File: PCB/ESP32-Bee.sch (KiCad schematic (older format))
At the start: 33 parts, among them J1 M22-2511005, J2 M22-2511005, SW1 B3U-1000P, T1 1909763-1, U1 ESP32, U2 W25Q64FWSSIG, X1 FA-128_26.0000MF10Z-AC3

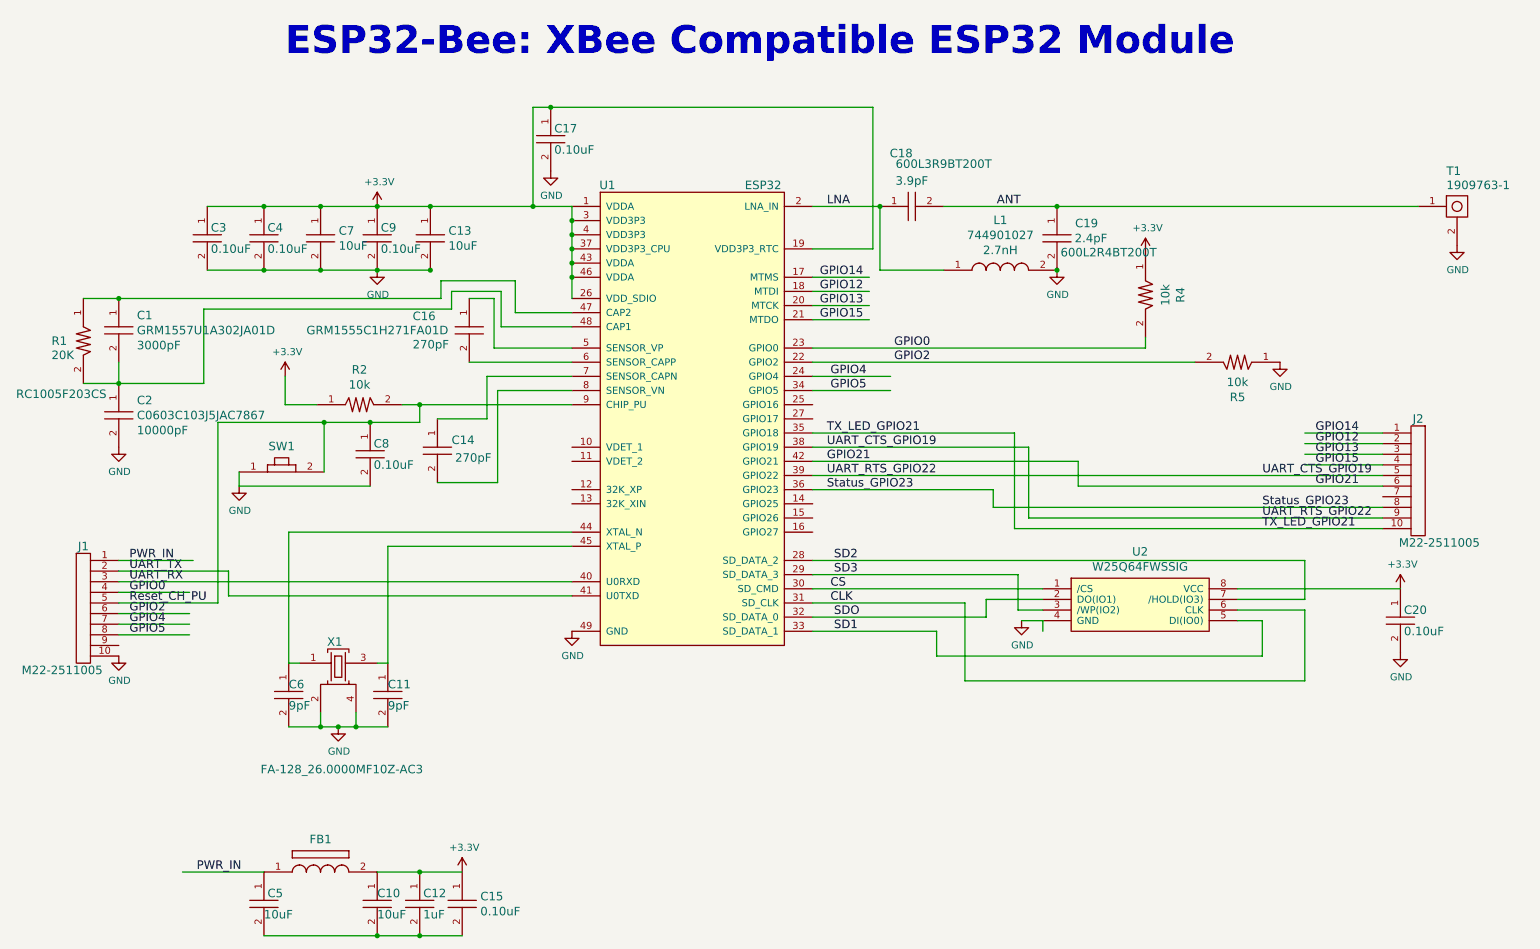
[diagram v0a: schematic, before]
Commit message: More Progress
More progress with the PCB, having a hard time finding a RF shielf that
is XBee pro sized.
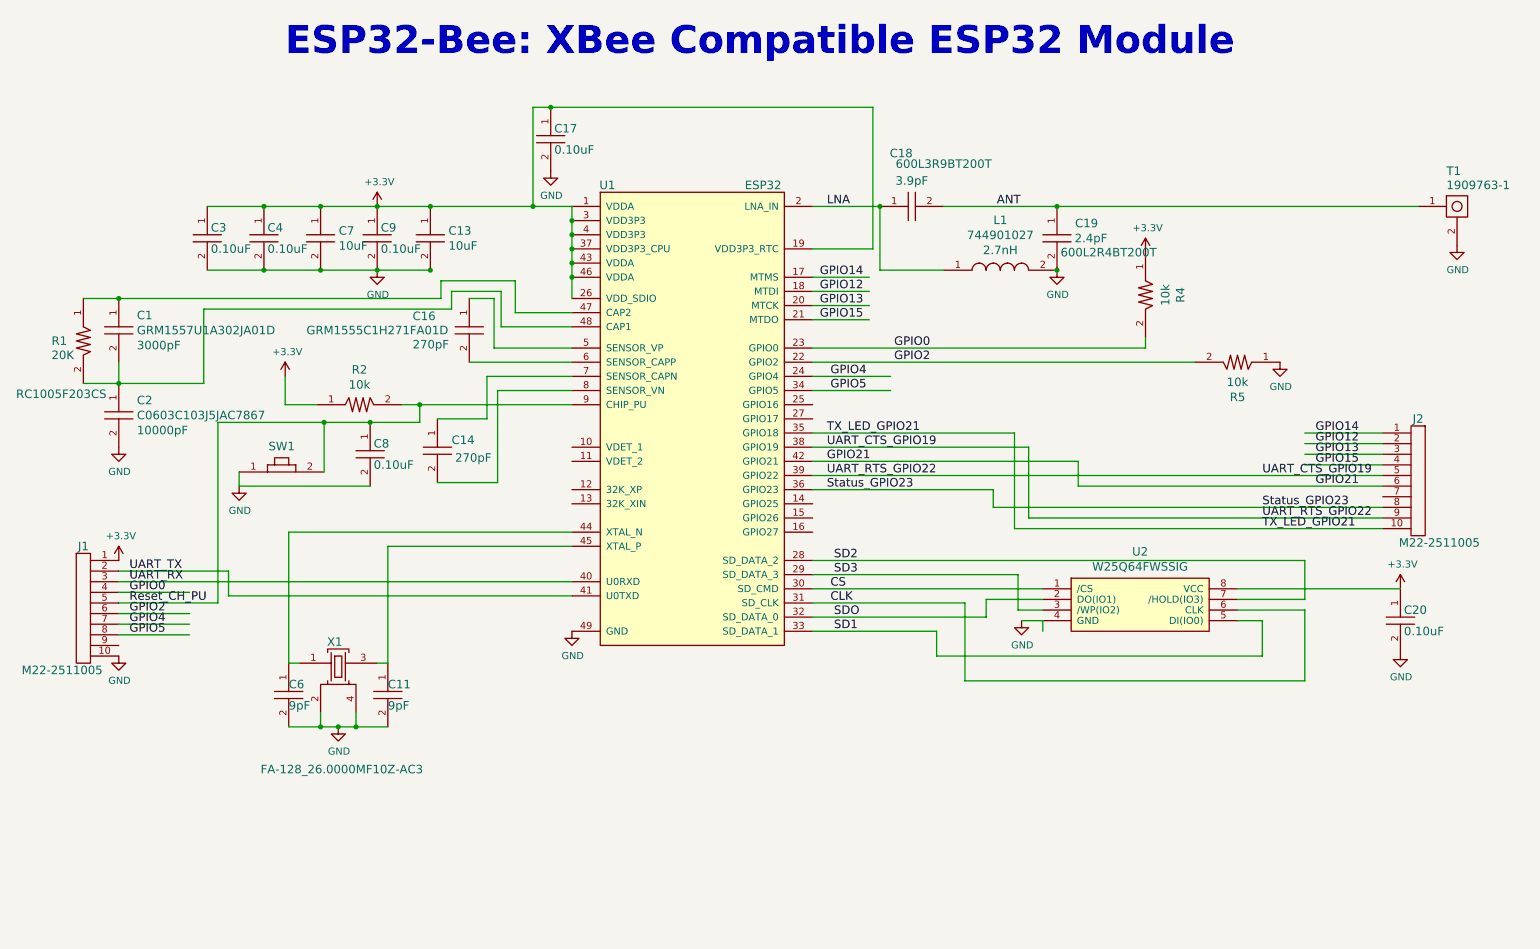
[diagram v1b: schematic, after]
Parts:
- removed C10, C5: CL10A106KQ8NNNC, PCB_Footprints:C0603, symbol CL10A106KQ8NNNC
- removed C12: CL05A105KA5NQNC, PCB_Footprints:C0402, symbol CL05A105KA5NQNC
- removed C15: CL05B104JP5NNNC, PCB_Footprints:C0402, symbol CL05B104JP5NNNC
- removed FB1: MI0603K300R-10, PCB_Footprints:MI0603K300R-10, symbol MI0603K300R-10
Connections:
- net labels removed: PWR_IN
- wire segments 114 -> 133
